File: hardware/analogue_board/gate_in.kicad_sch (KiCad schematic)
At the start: 46 parts, among them J801 Gate in holes, J802 Probe holes: PR1-10 100 kΩ, P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, U801 LM393DR2G, U802 LM393DR2G

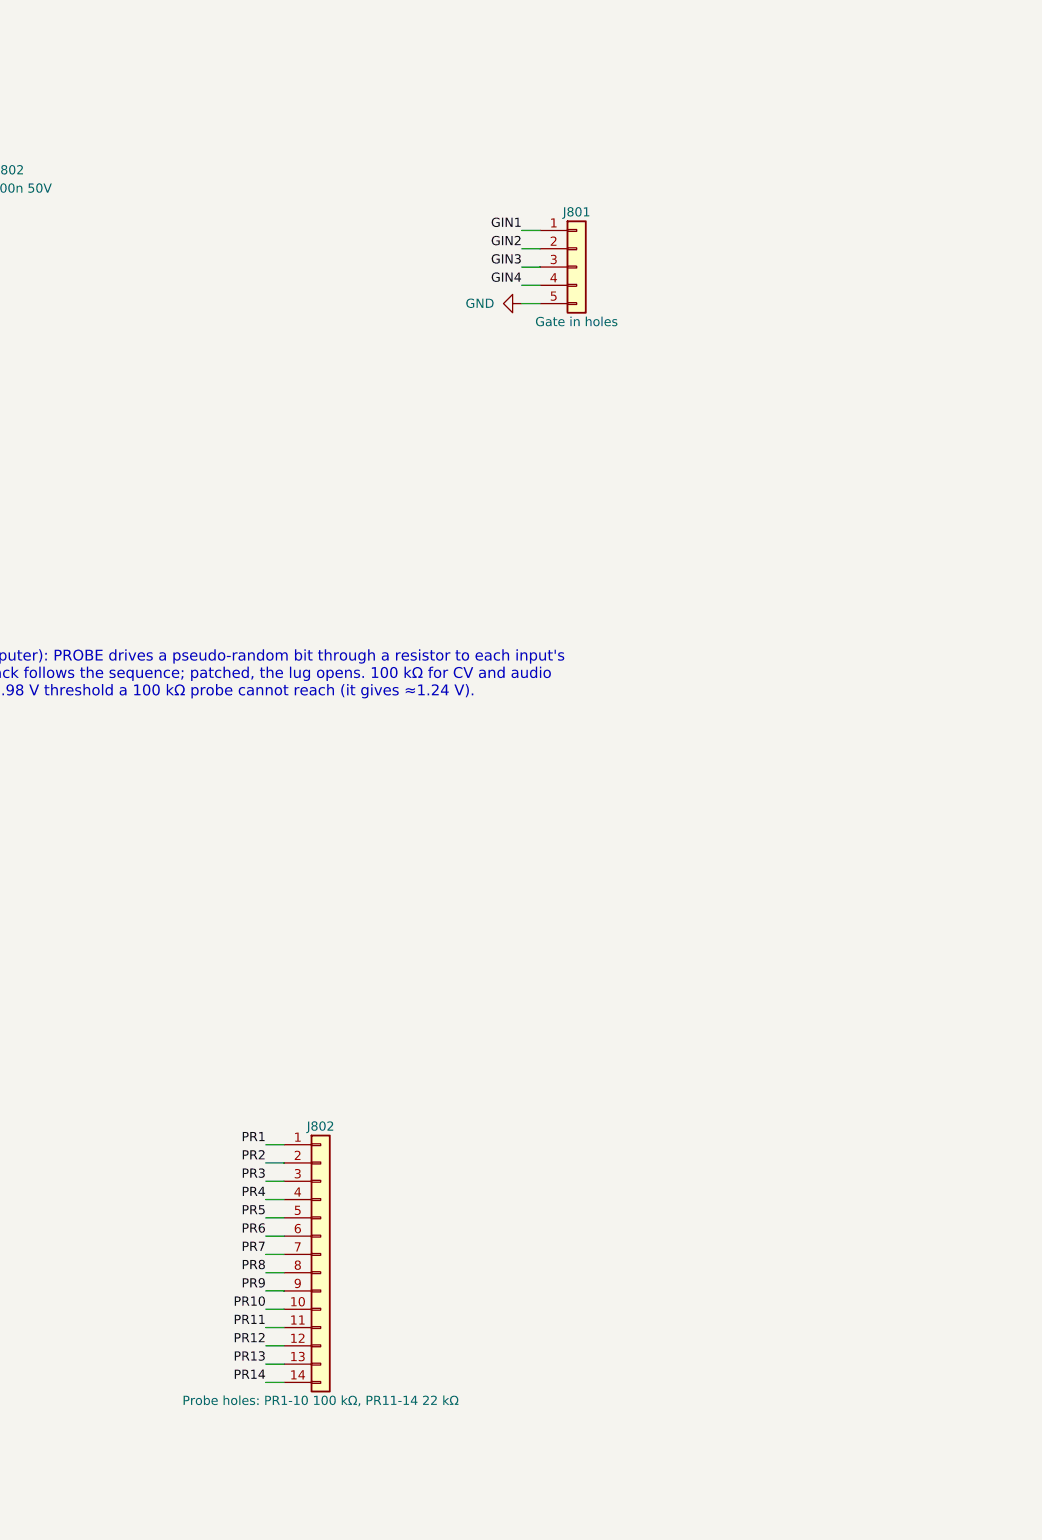
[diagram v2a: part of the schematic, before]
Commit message: Analogue board: first-pass placement; space reclaimed; four wiring banks
- autoplace.py places every unanchored part as close as it fits to the
  pins it connects to: decoupling capacitors at their pin, chains growing
  from their ICs, the buck's loop kept on one face. All 430 parts placed;
  DRC courtyards clean, schematic parity clean, heights checked (<= 2.5 mm
  under the modules, <= 8 mm in the USB keep-outs).
- Space reclaimed (David): Teensy socket without holes for its unused
  far-end pins 20-28 (headers 1x19 + 1x20); right strip (10HP only) without
  holes at 11-15 and 26-30, and outer hole only at 10, 16, 31. checks.py
  lets a project footprint omit only pins the netlist leaves unconnected.
- 74HCT595 in TSSOP-16 (74HCT595PW, C99710, same pinout) sideways in the
  right channel; vertical Qwiic socket (BM04B-SRSS-TB, C160390) below the
  modules, its cable straight up (the side-entry plug had no clear run).
- Wiring field as four mixed banks (David): each quarter of the board has
  some of every channel type, 50/50 left and right, jack-detect holes
  beside their inputs; wiring.py holds the plan, schematic and placement
  both read it. 94 holes.
- Reference designators off the silkscreen for passives and hole groups.

Co-Authored-By: Claude Opus 5.5 <noreply@anthropic.com>
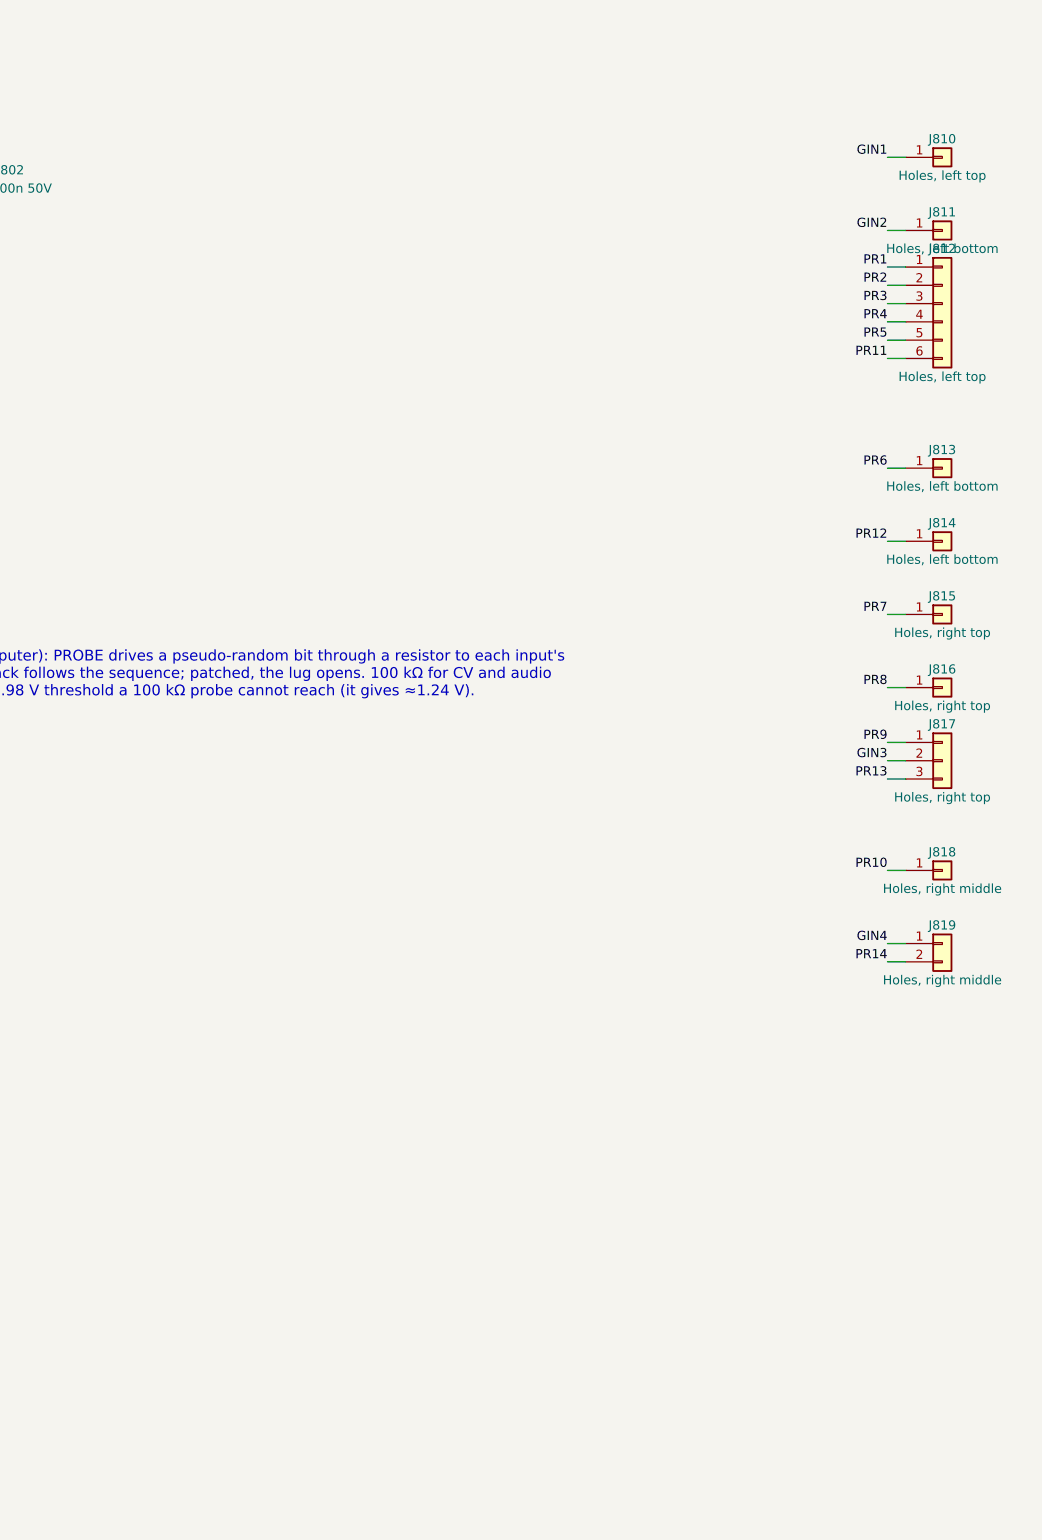
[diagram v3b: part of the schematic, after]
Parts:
- removed J802: Probe holes: PR1-10 100 kΩ, PR11-14 22 kΩ, analogue_board:WiringHoles_1x14, symbol Connector_Generic:Conn_01x14
- removed R833: 22k, Resistor_SMD:R_0402_1005Metric, symbol Device:R_Small
- added J811, J813, J814: Holes, left bottom, analogue_board:WiringHoles_1x01, symbol Connector_Generic:Conn_01x01
- added J812: Holes, left top, analogue_board:WiringHoles_1x06, symbol Connector_Generic:Conn_01x06
- added J816: Holes, right top, analogue_board:WiringHoles_1x01, symbol Connector_Generic:Conn_01x01
- added J817: Holes, right top, analogue_board:WiringHoles_1x03, symbol Connector_Generic:Conn_01x03
- added J818: Holes, right middle, analogue_board:WiringHoles_1x01, symbol Connector_Generic:Conn_01x01
- added R820, R824: 100k, Resistor_SMD:R_0402_1005Metric, symbol Device:R_Small
- added TP801: PROBE, TestPoint:TestPoint_Pad_D1.0mm, symbol Connector:TestPoint
- J810: renamed from J801; value Gate in holes -> Holes, left top; footprint analogue_board:WiringHoles_1x05 -> analogue_board:WiringHoles_1x01; symbol Connector_Generic:Conn_01x05 -> Connector_Generic:Conn_01x01
- J815: renamed from R820; value 100k -> Holes, right top; footprint Resistor_SMD:R_0402_1005Metric -> analogue_board:WiringHoles_1x01; symbol Device:R_Small -> Connector_Generic:Conn_01x01; JLC Basic -> bare holes; LCSC C25741 -> (none); Tolerance 1% -> (none); now left out of the parts list
- J819: renamed from R824; value 100k -> Holes, right middle; footprint Resistor_SMD:R_0402_1005Metric -> analogue_board:WiringHoles_1x02; symbol Device:R_Small -> Connector_Generic:Conn_01x02; JLC Basic -> bare holes; LCSC C25741 -> (none); Tolerance 1% -> (none); now left out of the parts list
- R833: renamed from TP801; value PROBE -> 22k; footprint TestPoint:TestPoint_Pad_D1.0mm -> Resistor_SMD:R_0402_1005Metric; symbol Connector:TestPoint -> Device:R_Small; JLC bare pad -> Basic; LCSC (none) -> C25768; Tolerance (none) -> 1%; now in the parts list
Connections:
- net GIN2: now also J811.1 (Pin_1); no longer J810.2 (Pin_2)
- net GIN3: now also J817.2 (Pin_2); no longer J810.3 (Pin_3)
- net GIN4: now also J819.1 (Pin_1); no longer J810.4 (Pin_4)
- net GND: no longer J810.5 (Pin_5)
- net PR1: now also J812.1 (Pin_1), R820.2; no longer J815.2
- net PR10: now also J818.1 (Pin_1)
- net PR11: now also J812.6 (Pin_6)
- net PR12: now also J814.1 (Pin_1)
- net PR13: now also J817.3 (Pin_3)
- net PR14: now also J819.2 (Pin_2), R833.2
- net PR2: now also J812.2 (Pin_2)
- net PR3: now also J812.3 (Pin_3)
- net PR4: now also J812.4 (Pin_4)
- net PR5: now also J812.5 (Pin_5), R824.2; no longer J819.2
- net PR6: now also J813.1 (Pin_1)
- net PR7: now also J815.1 (Pin_1)
- net PR8: now also J816.1 (Pin_1)
- net PR9: now also J817.1 (Pin_1)
- net PROBE: now also TP801.1; no longer R833.1
- net PROBE_BUS: now also R833.1, R820.1, R824.1; no longer J815.1, J819.1

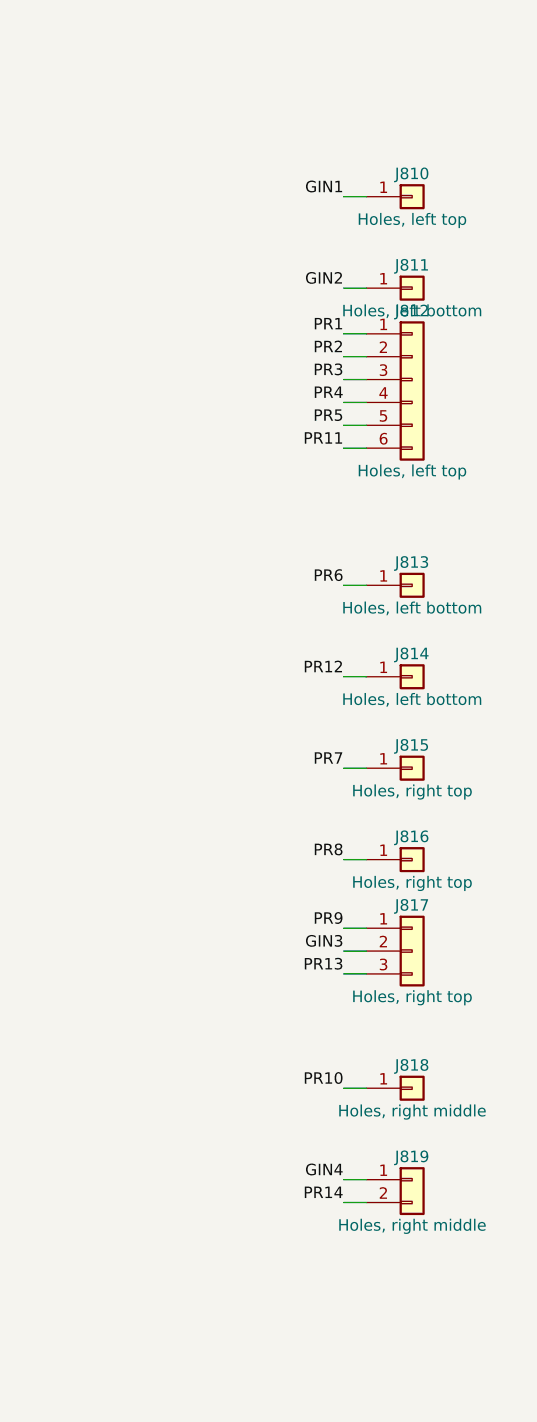
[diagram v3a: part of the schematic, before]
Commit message: Analogue board: bus chips level with their module pins; design rules; trial autoroute
Re-floorplan the centre channel in the order of the module's buses (SPI-A,
SPI-B, I2S, I2C), so the codec is 6 mm from the Pico's I2S pins instead of
38 mm; CV output op-amps move to the top-right corner.

Net classes (0.15/0.15 default, 0.3 power) and an In1 ground plane are
written into the project. autoroute.py runs Freerouting on a copy of the
board to measure routability. Schematic hole groups no longer overlap.

Co-Authored-By: Claude Opus 5.5 <noreply@anthropic.com>
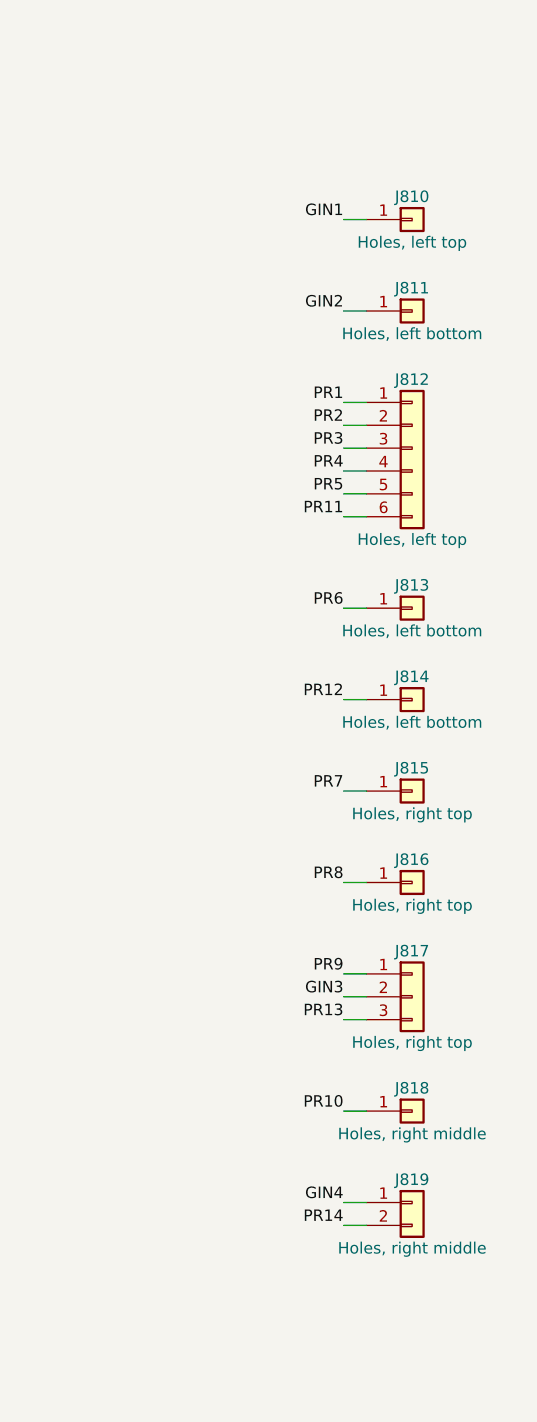
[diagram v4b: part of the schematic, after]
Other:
- moved on the sheet: J810, J811, J812, J813, J814, J815, J816, J817, J818, J819
